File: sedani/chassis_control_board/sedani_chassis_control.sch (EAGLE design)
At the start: 31 parts, among them J1 WIRELESS E-STOP, J10 OUTPUT 2, J11 OUTPUT 3, J12 SELECT, J13 ENCODER INPUT, J14 RC SERVO INPUT, J15 RC ESC INPUT, J16 RC BUTTON INPUT, J17 AUDIO BOARD POWER, J18 AUDIO BOARD INPUT, J19 SERVO OUTPUT, J2 E-STOP INTERFACE, J20 ESC OUTPUT, J3 MASTER 1, J4 MASTER 2, J5 MASTER 3, J6 SLAVE 1, J7 SLAVE 2, J8 SLAVE 3, J9 OUTPUT 1, T1 300mA

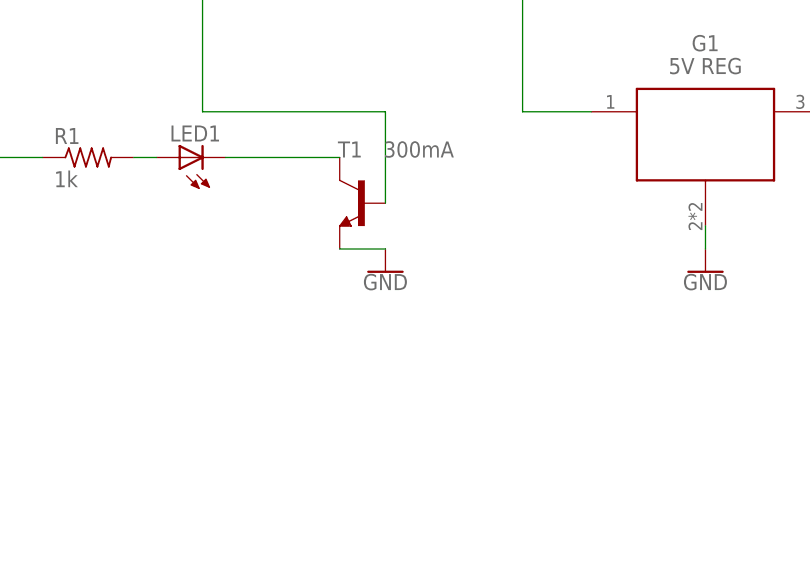
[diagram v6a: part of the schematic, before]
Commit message: added e-stop MOSFET gate resistor
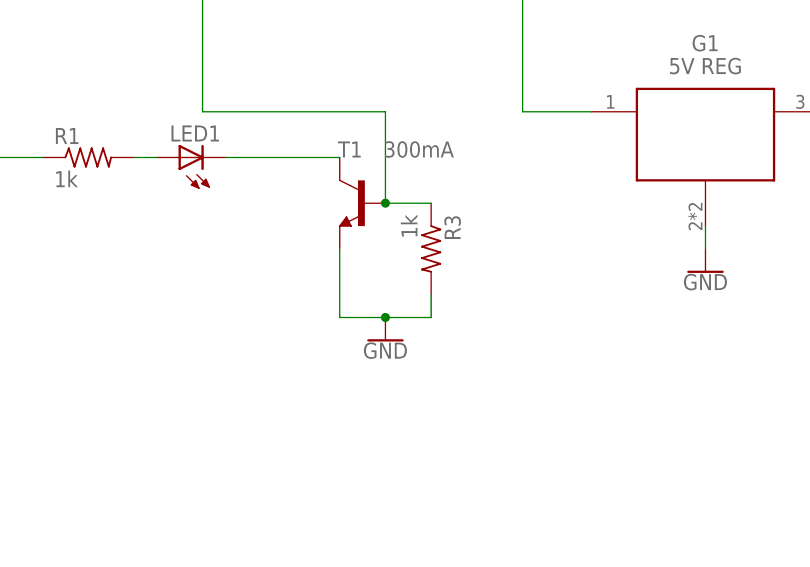
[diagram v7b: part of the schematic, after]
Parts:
- added R3: 1k, rcl:R-US_R0603
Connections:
- net E-STOP_OUTPUT: now also R3.1
- net GND: now also R3.2
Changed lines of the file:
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@@
 <part name="R2" library="rcl" library_urn="urn:adsk.eagle:library:334" deviceset="R-US_" device="R0603" package3d_urn="urn:adsk.eagle:package:23555/2" value="10k"/>
 <part name="RCVCC4" library="SparkFun-PowerSymbols" deviceset="VCC" device=""/>
+<part name="R3" library="rcl" library_urn="urn:adsk.eagle:library:334" deviceset="R-US_" device="R0603" package3d_urn="urn:adsk.eagle:package:23555/2" value="1k"/>
 </parts>
 <sheets>
@@
 <attribute name="VALUE" x="96.52" y="198.12" size="1.778" layer="96" rot="MR0"/>
 </instance>
-<instance part="GND8" gate="1" x="88.9" y="185.42" smashed="yes">
-<attribute name="VALUE" x="88.9" y="185.166" size="1.778" layer="96" align="top-center"/>
+<instance part="GND8" gate="1" x="88.9" y="177.8" smashed="yes">
+<attribute name="VALUE" x="88.9" y="177.546" size="1.778" layer="96" align="top-center"/>
 </instance>
 <instance part="LED1" gate="G$1" x="66.04" y="198.12" smashed="yes" rot="R90">
@@
 <instance part="RCVCC4" gate="G$1" x="45.72" y="198.12" smashed="yes" rot="R90">
 <attribute name="VALUE" x="42.926" y="198.12" size="1.778" layer="96" rot="R180" align="bottom-center"/>
+</instance>
+<instance part="R3" gate="G$1" x="93.98" y="187.96" smashed="yes" rot="R270">
+<attribute name="NAME" x="95.4786" y="191.77" size="1.778" layer="95" rot="R270"/>
+<attribute name="VALUE" x="90.678" y="191.77" size="1.778" layer="96" rot="R270"/>
 </instance>
 </instances>
@@
 </segment>
 <segment>
-<pinref part="GND8" gate="1" pin="GND"/>
-<pinref part="T1" gate="G$1" pin="E"/>
-<wire x1="88.9" y1="187.96" x2="83.82" y2="187.96" width="0.1524" layer="91"/>
-</segment>
-<segment>
 <pinref part="GND13" gate="1" pin="GND"/>
 <pinref part="S2" gate="G$1" pin="1"/>
 <wire x1="73.66" y1="101.6" x2="81.28" y2="101.6" width="0.1524" layer="91"/>
+</segment>
+<segment>
+<pinref part="R3" gate="G$1" pin="2"/>
+<pinref part="GND8" gate="1" pin="GND"/>
+<wire x1="93.98" y1="182.88" x2="93.98" y2="180.34" width="0.1524" layer="91"/>
+<wire x1="93.98" y1="180.34" x2="88.9" y2="180.34" width="0.1524" layer="91"/>
+<pinref part="T1" gate="G$1" pin="E"/>
+<wire x1="83.82" y1="187.96" x2="83.82" y2="180.34" width="0.1524" layer="91"/>
+<wire x1="83.82" y1="180.34" x2="88.9" y2="180.34" width="0.1524" layer="91"/>
+<junction x="88.9" y="180.34"/>
 </segment>
 </net>
@@
 <pinref part="T1" gate="G$1" pin="B"/>
 <wire x1="88.9" y1="203.2" x2="88.9" y2="193.04" width="0.1524" layer="91"/>
-</segment>
-</net>
+<pinref part="R3" gate="G$1" pin="1"/>
+<wire x1="88.9" y1="193.04" x2="93.98" y2="193.04" width="0.1524" layer="91"/>
+<junction x="88.9" y="193.04"/>
+</segment>
+</net>

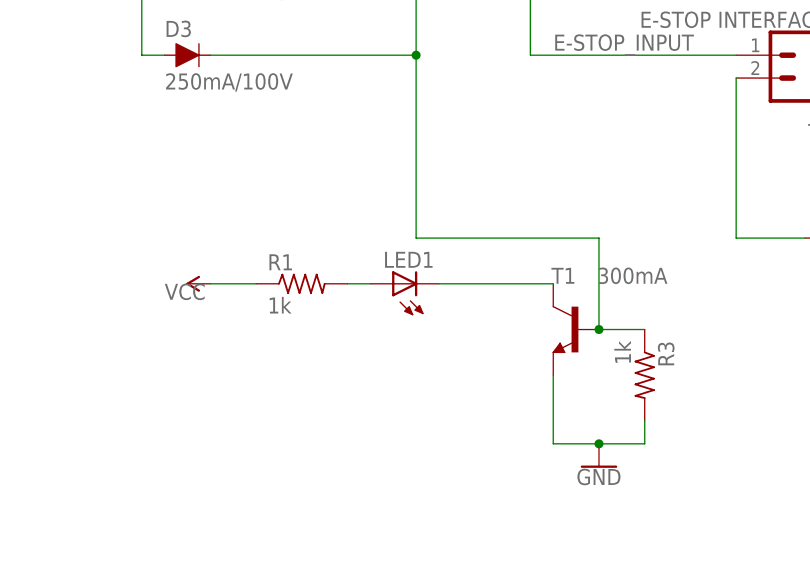
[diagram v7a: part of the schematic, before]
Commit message: finished routing, pending redesigned 5V regulator
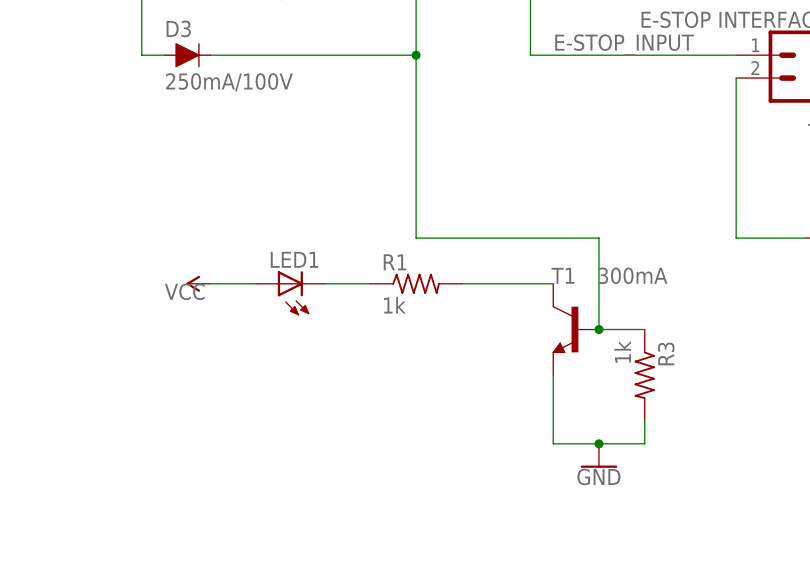
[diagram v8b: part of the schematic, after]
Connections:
- removed net N$3: LED1.A, R1.2
- new net N$2: R1.2, T1.C
- net N$1: now also R1.1; no longer T1.C
- net VCC: now also LED1.A; no longer R1.1
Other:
- moved on the sheet: LED1, R1
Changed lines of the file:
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@@
 <attribute name="VALUE" x="88.9" y="177.546" size="1.778" layer="96" align="top-center"/>
 </instance>
-<instance part="LED1" gate="G$1" x="66.04" y="198.12" smashed="yes" rot="R90">
-<attribute name="NAME" x="70.612" y="201.676" size="1.778" layer="95" rot="R180"/>
-<attribute name="VALUE" x="70.612" y="203.835" size="1.778" layer="96" rot="R180"/>
-</instance>
-<instance part="R1" gate="G$1" x="55.88" y="198.12" smashed="yes">
-<attribute name="NAME" x="52.07" y="199.6186" size="1.778" layer="95"/>
-<attribute name="VALUE" x="52.07" y="194.818" size="1.778" layer="96"/>
+<instance part="LED1" gate="G$1" x="53.34" y="198.12" smashed="yes" rot="R90">
+<attribute name="NAME" x="57.912" y="201.676" size="1.778" layer="95" rot="R180"/>
+<attribute name="VALUE" x="57.912" y="203.835" size="1.778" layer="96" rot="R180"/>
+</instance>
+<instance part="R1" gate="G$1" x="68.58" y="198.12" smashed="yes">
+<attribute name="NAME" x="64.77" y="199.6186" size="1.778" layer="95"/>
+<attribute name="VALUE" x="64.77" y="194.818" size="1.778" layer="96"/>
 </instance>
 <instance part="S2" gate="G$1" x="86.36" y="101.6" smashed="yes">
@@
 <segment>
 <pinref part="RCVCC4" gate="G$1" pin="VCC"/>
-<pinref part="R1" gate="G$1" pin="1"/>
+<pinref part="LED1" gate="G$1" pin="A"/>
 <wire x1="45.72" y1="198.12" x2="50.8" y2="198.12" width="0.1524" layer="91"/>
 </segment>
@@
 </segment>
 </net>
-<net name="N$3" class="0">
-<segment>
-<pinref part="R1" gate="G$1" pin="2"/>
-<pinref part="LED1" gate="G$1" pin="A"/>
-<wire x1="60.96" y1="198.12" x2="63.5" y2="198.12" width="0.1524" layer="91"/>
-</segment>
-</net>
 <net name="ARDUINO_RST" class="0">
 <segment>
@@
 <segment>
 <pinref part="LED1" gate="G$1" pin="C"/>
+<pinref part="R1" gate="G$1" pin="1"/>
+<wire x1="58.42" y1="198.12" x2="63.5" y2="198.12" width="0.1524" layer="91"/>
+</segment>
+</net>
+<net name="N$2" class="0">
+<segment>
+<pinref part="R1" gate="G$1" pin="2"/>
 <pinref part="T1" gate="G$1" pin="C"/>
-<wire x1="71.12" y1="198.12" x2="83.82" y2="198.12" width="0.1524" layer="91"/>
-</segment>
-</net>
+<wire x1="73.66" y1="198.12" x2="83.82" y2="198.12" width="0.1524" layer="91"/>
+</segment>
+</net>
